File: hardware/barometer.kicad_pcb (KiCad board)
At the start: 2 copper layers, 15 x 25 mm, 26 parts, among them P1 CON-SENSOR2, P2 CONN_01X01, P3 BOOT, U1 XMC1XXX24, U2 LPS22HB, U3 DRILL, U4 DRILL, U5 DRILL, U6 DRILL

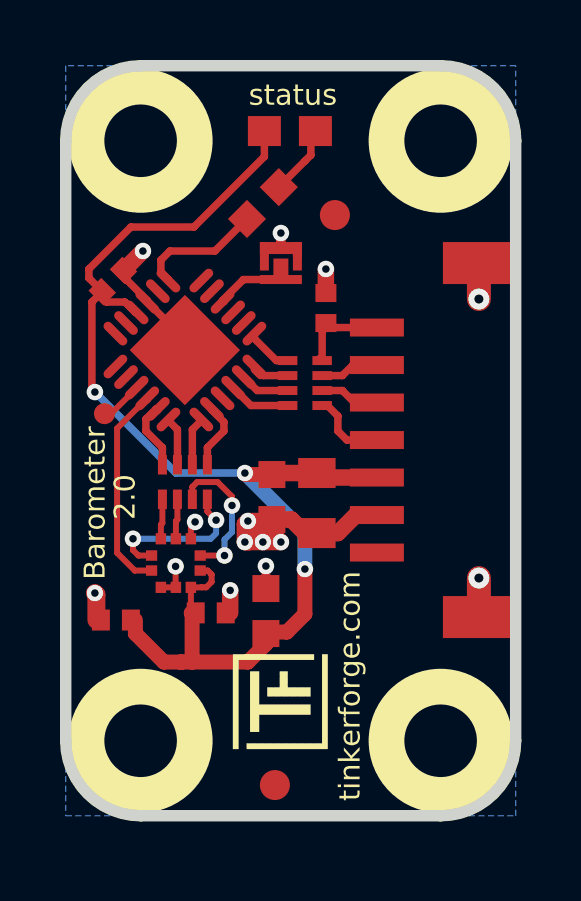
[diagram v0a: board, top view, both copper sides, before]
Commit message: fix sensor footprint
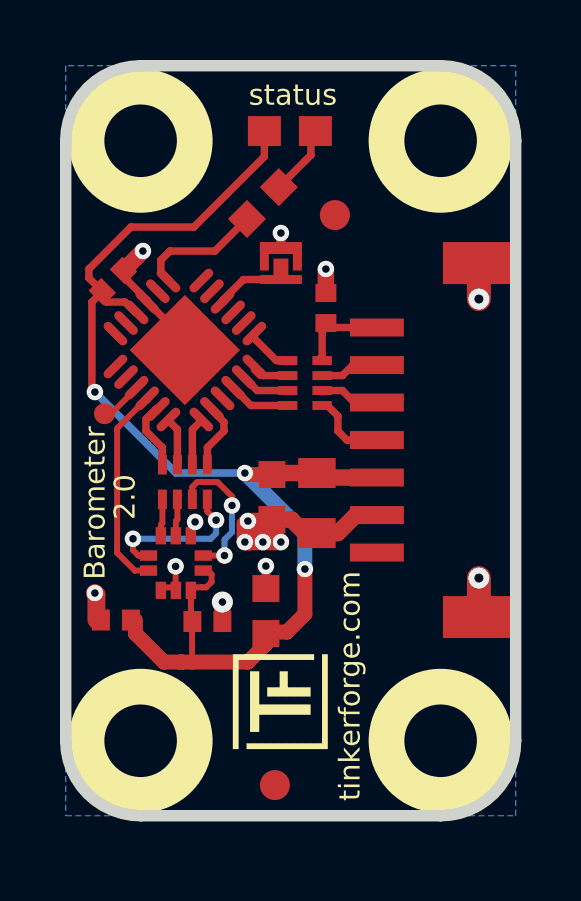
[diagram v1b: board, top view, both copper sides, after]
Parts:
- moved C6 0.31 mm to (145.1, 109.2)
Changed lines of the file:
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@@
-(kicad_pcb (version 4) (host pcbnew 4.0.2+dfsg1-stable)
+(kicad_pcb (version 4) (host pcbnew 4.0.7-e2-6376~58~ubuntu17.04.1)
   (general
     (links 53)
     (no_connects 0)
-    (area 140.136879 90.431619 155.519121 115.813841)
+    (area 139.469339 89.769159 284.64585 166.140793)
     (thickness 1.6002)
     (drawings 13)
@@
   )
   (setup
-    (last_trace_width 0.29972)
+    (last_trace_width 0.2)
     (user_trace_width 0.2)
     (user_trace_width 0.25)
@@
   )
   (module kicad-libraries:C0402F (layer Vorderseite)
-    (at 145.16 108.86)
+    (at 145.05 109.15)
     (fp_text reference C6 (at 0.1 0.15) (layer F.Fab)
       (effects (font (size 0.2 0.2) (thickness 0.05)))
@@
     (fp_line (start 1 1) (end -1 1) (layer F.Fab) (width 0.05))
     (fp_line (start -1 1) (end -1 -1) (layer F.Fab) (width 0.05))
-    (pad 4 smd rect (at 0 -0.81) (size 0.35 0.375) (layers Vorderseite F.Paste F.Mask)
+    (pad 4 smd rect (at 0 -0.91) (size 0.35 0.575) (layers Vorderseite F.Paste F.Mask)
       (net 15 M-MOSI))
-    (pad 3 smd rect (at 0.5 -0.81) (size 0.35 0.375) (layers Vorderseite F.Paste F.Mask)
+    (pad 3 smd rect (at 0.5 -0.91) (size 0.35 0.575) (layers Vorderseite F.Paste F.Mask)
       (net 1 GND))
-    (pad 5 smd rect (at -0.5 -0.81) (size 0.35 0.375) (layers Vorderseite F.Paste F.Mask)
+    (pad 5 smd rect (at -0.5 -0.91) (size 0.35 0.575) (layers Vorderseite F.Paste F.Mask)
       (net 14 M-MISO))
-    (pad 9 smd rect (at 0 0.81) (size 0.35 0.375) (layers Vorderseite F.Paste F.Mask)
+    (pad 9 smd rect (at 0 0.91) (size 0.35 0.575) (layers Vorderseite F.Paste F.Mask)
       (net 1 GND))
-    (pad 10 smd rect (at 0.5 0.81) (size 0.35 0.375) (layers Vorderseite F.Paste F.Mask)
+    (pad 10 smd rect (at 0.5 0.91) (size 0.35 0.575) (layers Vorderseite F.Paste F.Mask)
       (net 2 VCC))
-    (pad 8 smd rect (at -0.5 0.81) (size 0.35 0.375) (layers Vorderseite F.Paste F.Mask)
+    (pad 8 smd rect (at -0.5 0.91) (size 0.35 0.575) (layers Vorderseite F.Paste F.Mask)
       (net 1 GND))
-    (pad 6 smd rect (at -0.81 -0.25 90) (size 0.35 0.375) (layers Vorderseite F.Paste F.Mask)
+    (pad 6 smd rect (at -0.91 -0.25 90) (size 0.35 0.575) (layers Vorderseite F.Paste F.Mask)
       (net 17 M-CS))
-    (pad 7 smd rect (at -0.81 0.25 90) (size 0.35 0.375) (layers Vorderseite F.Paste F.Mask)
+    (pad 7 smd rect (at -0.91 0.25 90) (size 0.35 0.575) (layers Vorderseite F.Paste F.Mask)
       (net 23 INT))
-    (pad 2 smd rect (at 0.81 -0.25 90) (size 0.35 0.375) (layers Vorderseite F.Paste F.Mask)
+    (pad 2 smd rect (at 0.91 -0.25 90) (size 0.35 0.575) (layers Vorderseite F.Paste F.Mask)
       (net 16 M-CLK))
-    (pad 1 smd rect (at 0.81 0.25 90) (size 0.35 0.375) (layers Vorderseite F.Paste F.Mask)
+    (pad 1 smd rect (at 0.91 0.25 90) (size 0.35 0.575) (layers Vorderseite F.Paste F.Mask)
       (net 2 VCC))
     (model Sensors_Detectors/LPS22HB_HLGA-10L.wrl
@@
     (effects (font (size 0.7 0.7) (thickness 0.15)))
   )
+  (segment (start 145.55 109.15) (end 145.55 108.5) (width 0.55) (layer Vorderseite) (net 1))
+  (via (at 145.55 108.5) (size 0.70104) (drill 0.24892) (layers Vorderseite Rückseite) (net 1))
   (segment (start 146.95 96.975) (end 146.95 96.7) (width 0.2) (layer Vorderseite) (net 1))
   (segment (start 146.95 96.7) (end 147.5 96.7) (width 0.2) (layer Vorderseite) (net 1))
@@
   (via (at 147.5 96.2) (size 0.55) (drill 0.25) (layers Vorderseite Rückseite) (net 1))
   (segment (start 147.5 96.7) (end 147.5 96.2) (width 0.29972) (layer Vorderseite) (net 1))
-  (segment (start 145.81 108.86) (end 145.81 108.11) (width 0.55) (layer Vorderseite) (net 1))
-  (via (at 145.81 108.11) (size 0.55) (drill 0.25) (layers Vorderseite Rückseite) (net 1))
   (segment (start 144.5 106.39) (end 144.5 105.97) (width 0.2) (layer Vorderseite) (net 1))
   (via (at 144.64 105.83) (size 0.55) (drill 0.25) (layers Vorderseite Rückseite) (net 1))
@@
   (segment (start 144.5 108.01) (end 144.5 108.85) (width 0.2) (layer Vorderseite) (net 2))
   (segment (start 144.5 108.85) (end 144.51 108.86) (width 0.2) (layer Vorderseite) (net 2))
-  (segment (start 144.54 110.5) (end 144.54 108.89) (width 0.5) (layer Vorderseite) (net 2))
-  (segment (start 144.54 108.89) (end 144.51 108.86) (width 0.5) (layer Vorderseite) (net 2))
+  (segment (start 144.54 110.5) (end 144.54 108.89) (width 0.2) (layer Vorderseite) (net 2))
+  (segment (start 144.54 108.89) (end 144.51 108.86) (width 0.2) (layer Vorderseite) (net 2))
   (segment (start 146.3 104.2) (end 144 104.2) (width 0.25) (layer Rückseite) (net 2))
   (segment (start 141.2 101.4) (end 141.2 98.5) (width 0.25) (layer Vorderseite) (net 2))
